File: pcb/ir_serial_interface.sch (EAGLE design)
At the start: 27 parts, among them IC1 PIC18F2550_28W, IC2 LP2992, Q2 BC847SMD, T1 PS401

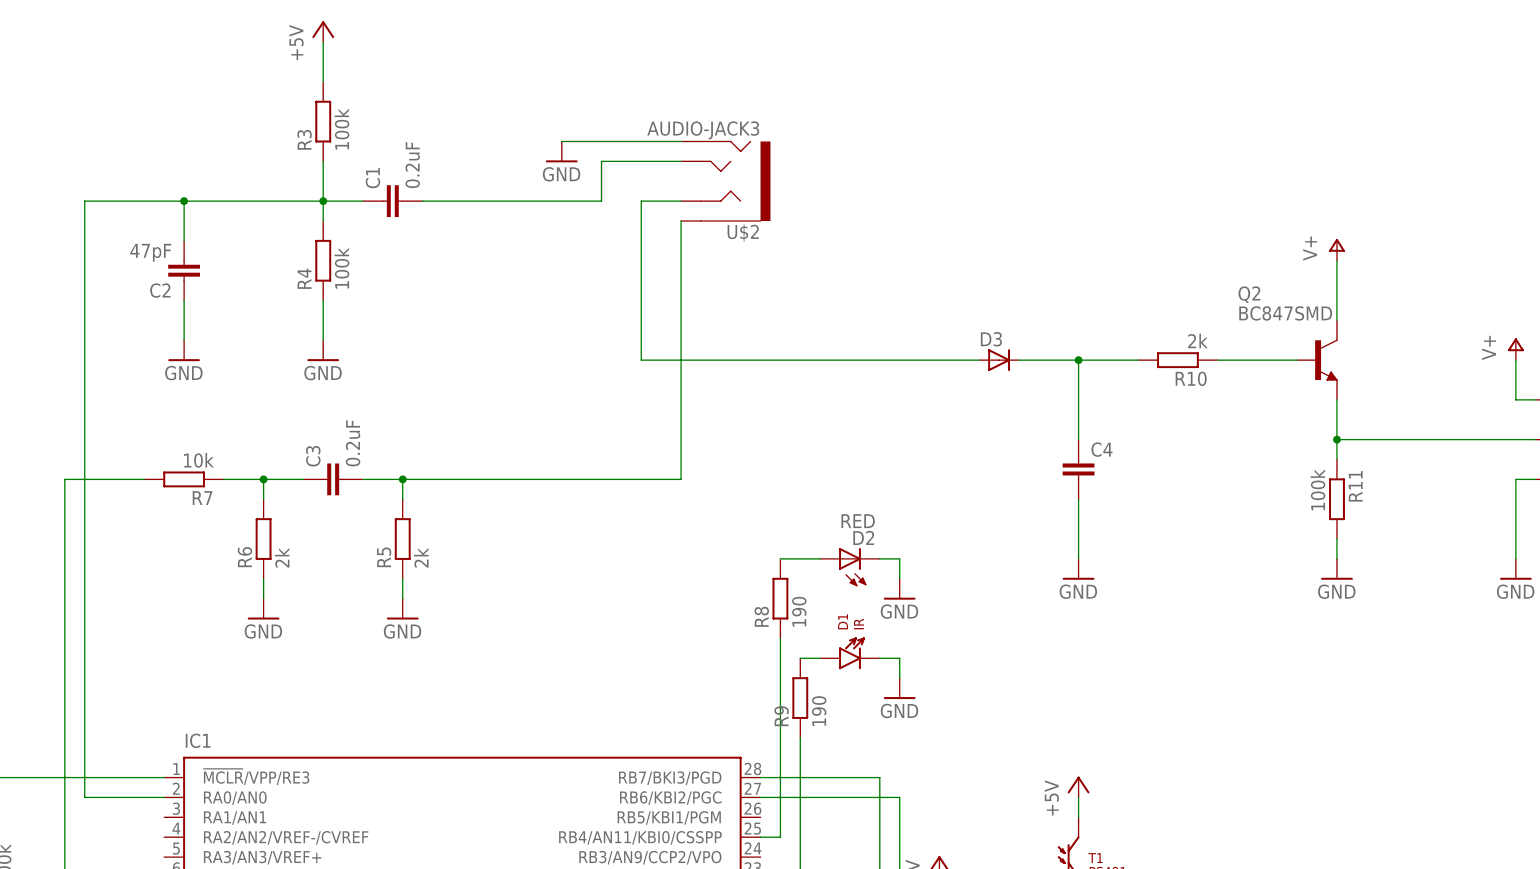
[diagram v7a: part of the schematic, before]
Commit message: silk screen on name layer not value layer
+ component values
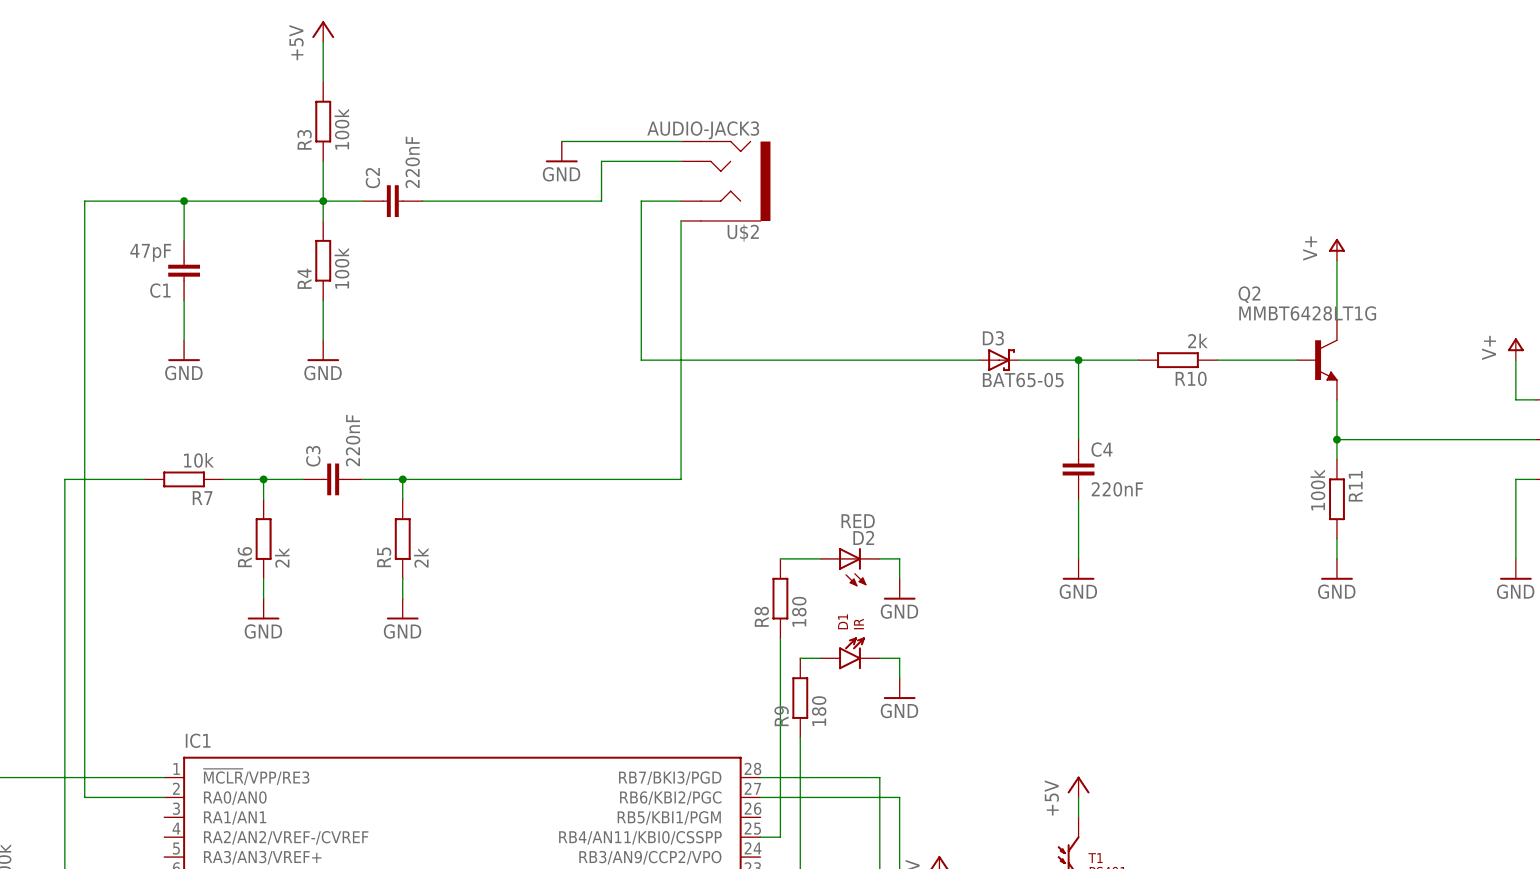
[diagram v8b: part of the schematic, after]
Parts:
- C1: value 0.2uF -> 47pF
- C2: value 47pF -> 220nF
- C3: value 0.2uF -> 220nF
- C4: value (none) -> 220nF
- D3: value (none) -> BAT65-05; device semicon-smd-ipc:D-A1-C3 -> diode:BAT54
- Q2: value BC847SMD -> MMBT6428LT1G
- R8, R9: value 190 -> 180
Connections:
- net GND: now also C1.1; no longer C2.1
- net N$5: now also C2.2; no longer C1.2
- net N$6: now also C1.2, C2.1; no longer C1.1, C2.2
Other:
- moved on the sheet: C1, C2
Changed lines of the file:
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@@
 <part name="R1" library="resistor" deviceset="R-EU_" device="M0805" value="10k"/>
 <part name="R3" library="resistor" deviceset="R-EU_" device="M0805" value="100k"/>
-<part name="C1" library="SparkFun (old)" deviceset="CAP" device="0805" value="0.2uF"/>
+<part name="C2" library="SparkFun (old)" deviceset="CAP" device="0805" value="220nF"/>
 <part name="IC1" library="microchip" deviceset="PIC18F2*_28" device="W" technology="550"/>
-<part name="C2" library="SparkFun (old)" deviceset="CAP" device="0805" value="47pF"/>
+<part name="C1" library="SparkFun (old)" deviceset="CAP" device="0805" value="47pF"/>
 <part name="P+4" library="supply1" deviceset="+5V" device=""/>
 <part name="GND5" library="supply1" deviceset="GND" device=""/>
 <part name="GND6" library="supply1" deviceset="GND" device=""/>
-<part name="C3" library="SparkFun (old)" deviceset="CAP" device="0805" value="0.2uF"/>
+<part name="C3" library="SparkFun (old)" deviceset="CAP" device="0805" value="220nF"/>
 <part name="R5" library="resistor" deviceset="R-EU_" device="M0805" value="2k"/>
 <part name="R6" library="resistor" deviceset="R-EU_" device="M0805" value="2k"/>
@@
 <part name="D2" library="SparkFun-LED" deviceset="LED-RED" device="LILYPAD" value="RED"/>
 <part name="GND9" library="supply1" deviceset="GND" device=""/>
-<part name="R8" library="resistor" deviceset="R-EU_" device="M0805" value="190"/>
+<part name="R8" library="resistor" deviceset="R-EU_" device="M0805" value="180"/>
 <part name="BAT1" library="SparkFun-Electromechanical" deviceset="BATTERY" device="20PTH" value="20mm coincell"/>
 <part name="P+5" library="supply1" deviceset="+5V" device=""/>
 <part name="GND10" library="supply1" deviceset="GND" device=""/>
-<part name="R9" library="resistor" deviceset="R-EU_" device="M0805" value="190"/>
+<part name="R9" library="resistor" deviceset="R-EU_" device="M0805" value="180"/>
 <part name="D1" library="SparkFun-LED" deviceset="LTE-302" device="" value="IR"/>
 <part name="GND11" library="supply1" deviceset="GND" device=""/>
-<part name="C4" library="rcl" deviceset="C-EU" device="C0805"/>
+<part name="C4" library="rcl" deviceset="C-EU" device="C0805" value="220nF"/>
 <part name="R4" library="resistor" deviceset="R-EU_" device="M0805" value="100k"/>
 <part name="U$2" library="SparkFun-Connectors" deviceset="AUDIO-JACK3" device=""/>
 <part name="GND12" library="supply1" deviceset="GND" device=""/>
-<part name="Q2" library="transistor-npn" deviceset="BC847*" device="SMD"/>
-<part name="D3" library="semicon-smd-ipc" deviceset="D-" device="A1-C3"/>
+<part name="Q2" library="transistor-npn" deviceset="BC847*" device="SMD" value="MMBT6428LT1G"/>
+<part name="D3" library="diode" deviceset="BAT54" device="" value="BAT65-05"/>
 <part name="GND4" library="supply1" deviceset="GND" device=""/>
 <part name="R10" library="resistor" deviceset="R-EU_" device="M0805" value="2k"/>
@@
 <instance part="R1" gate="G$1" x="15.24" y="10.16" rot="R180"/>
 <instance part="R3" gate="G$1" x="76.2" y="121.92" rot="R90"/>
-<instance part="C1" gate="G$1" x="86.36" y="111.76" rot="R90"/>
+<instance part="C2" gate="G$1" x="86.36" y="111.76" rot="R90"/>
 <instance part="IC1" gate="G$1" x="93.98" y="22.86"/>
-<instance part="C2" gate="G$1" x="58.42" y="104.14" rot="R180"/>
+<instance part="C1" gate="G$1" x="58.42" y="104.14" rot="R180"/>
 <instance part="P+4" gate="1" x="76.2" y="134.62"/>
 <instance part="GND5" gate="1" x="76.2" y="91.44"/>
@@
 </segment>
 <segment>
-<pinref part="C2" gate="G$1" pin="1"/>
+<pinref part="C1" gate="G$1" pin="1"/>
 <pinref part="GND6" gate="1" pin="GND"/>
 <wire x1="58.42" y1="99.06" x2="58.42" y2="93.98" width="0.1524" layer="91"/>
@@
 <pinref part="R3" gate="G$1" pin="1"/>
 <wire x1="76.2" y1="116.84" x2="76.2" y2="111.76" width="0.1524" layer="91"/>
-<pinref part="C1" gate="G$1" pin="1"/>
+<pinref part="C2" gate="G$1" pin="1"/>
 <wire x1="81.28" y1="111.76" x2="76.2" y2="111.76" width="0.1524" layer="91"/>
 <junction x="76.2" y="111.76"/>
-<pinref part="C2" gate="G$1" pin="2"/>
+<pinref part="C1" gate="G$1" pin="2"/>
 <wire x1="76.2" y1="111.76" x2="58.42" y2="111.76" width="0.1524" layer="91"/>
 <wire x1="58.42" y1="111.76" x2="58.42" y2="106.68" width="0.1524" layer="91"/>
@@
 <wire x1="111.76" y1="116.84" x2="121.92" y2="116.84" width="0.1524" layer="91"/>
 <wire x1="111.76" y1="116.84" x2="111.76" y2="111.76" width="0.1524" layer="91"/>
-<pinref part="C1" gate="G$1" pin="2"/>
+<pinref part="C2" gate="G$1" pin="2"/>
 <wire x1="111.76" y1="111.76" x2="88.9" y2="111.76" width="0.1524" layer="91"/>
 </segment>
